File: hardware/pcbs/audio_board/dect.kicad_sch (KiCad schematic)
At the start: 9 parts, among them M1 DHAN-M_Module

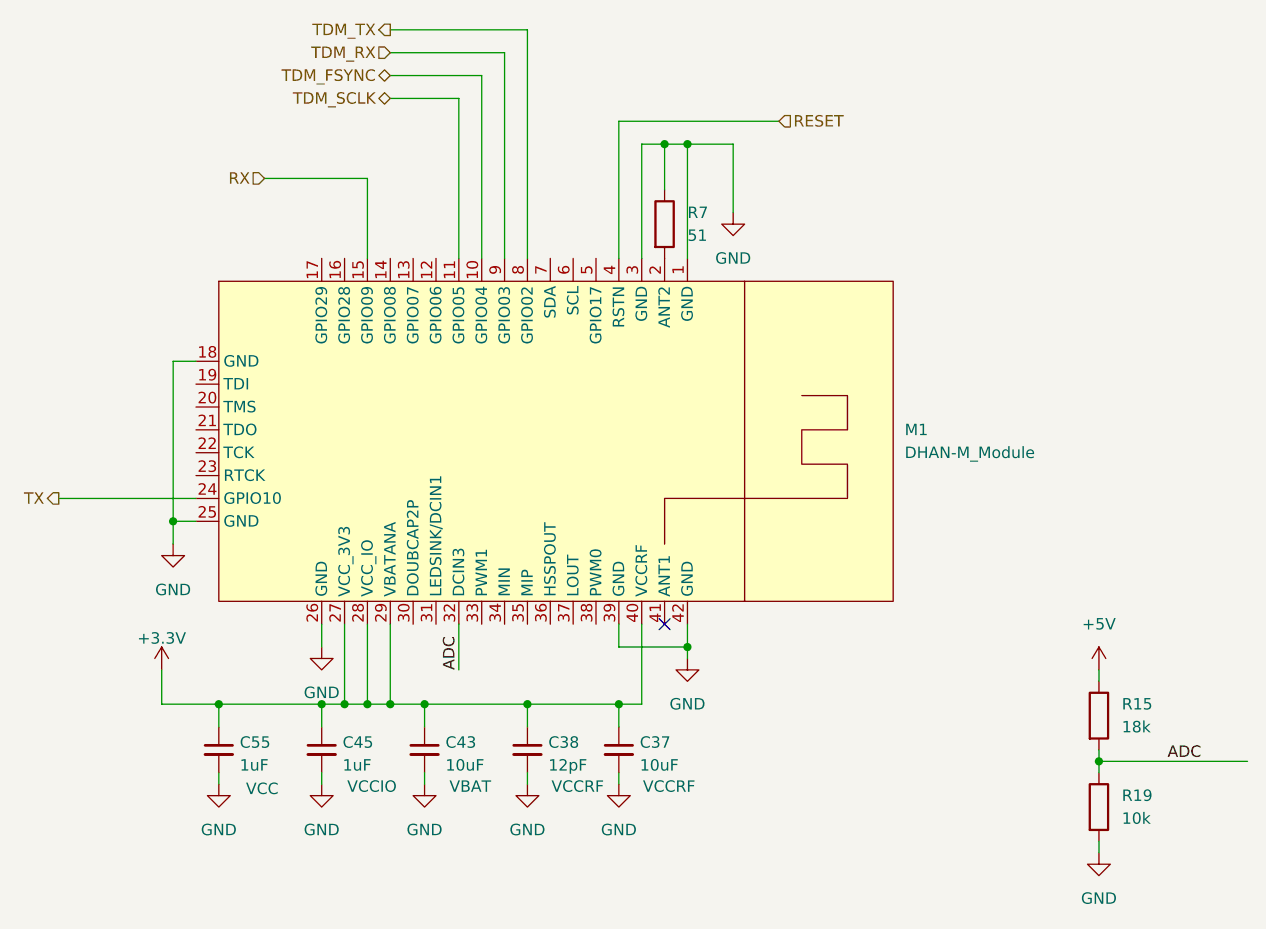
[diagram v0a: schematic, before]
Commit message: audio_board: Rework for DECT plug-in module
Redesigned the DECT area to accept a daughterboard with whatever DECT
module ends up working. Added more holes and silkscreen to make the
board neater.
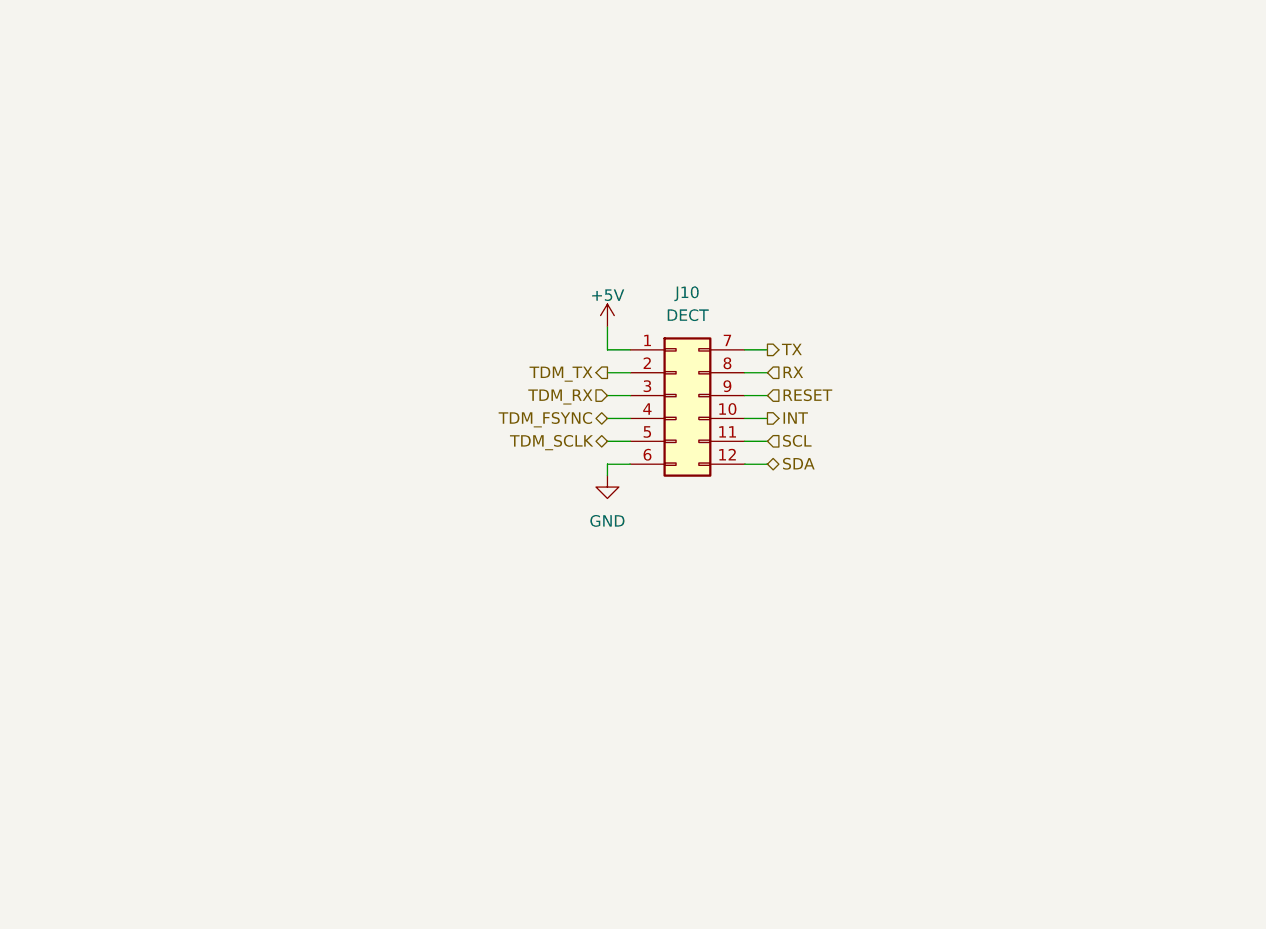
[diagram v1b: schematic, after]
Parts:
- removed C37, C43: 10uF, Capacitor_SMD:C_0805_2012Metric_Pad1.18x1.45mm_HandSolder, symbol Device:C_Small
- removed C38: 12pF, Capacitor_SMD:C_0603_1608Metric_Pad1.08x0.95mm_HandSolder, symbol Device:C_Small
- removed C45, C55: 1uF, Capacitor_SMD:C_0603_1608Metric_Pad1.08x0.95mm_HandSolder, symbol Device:C_Small
- removed M1: DHAN-M_Module, Library:DHAN-M_Module, symbol Parts:DHAN-M_Module
- removed R15: 18k, Resistor_SMD:R_0603_1608Metric_Pad0.98x0.95mm_HandSolder, symbol Device:R
- removed R19: 10k, Resistor_SMD:R_0603_1608Metric_Pad0.98x0.95mm_HandSolder, symbol Device:R
- removed R7: 51, Resistor_SMD:R_0603_1608Metric_Pad0.98x0.95mm_HandSolder, symbol Device:R
- added J10: DECT, Library:DectModule, symbol Connector_Generic:Conn_02x06_Top_Bottom
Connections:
- net +5V: now also J10.1 (Pin_1)
- net GND: now also J10.6 (Pin_6)
- net RESET: now also J10.9 (Pin_9)
- net RX: now also J10.8 (Pin_8)
- net TDM_FSYNC: now also J10.4 (Pin_4)
- net TDM_RX: now also J10.3 (Pin_3)
- net TDM_SCLK: now also J10.5 (Pin_5)
- net TDM_TX: now also J10.2 (Pin_2)
- net TX: now also J10.7 (Pin_7)
- new net INT: J10.10 (Pin_10)
- new net SCL: J10.11 (Pin_11)
- new net SDA: J10.12 (Pin_12)
- no-connect marks 1 -> 0

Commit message: audio_board, power_board: update shop and part links
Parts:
- J10: Part (none) -> 2x Header_2x06
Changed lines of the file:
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@@
+			)
+		)
+		(property "Part" "2x Header_2x06"
+			(at 153.67 99.06 0)
+			(effects
+				(font
+					(size 1.27 1.27)
+				)
+				(hide yes)
 			)
 		)

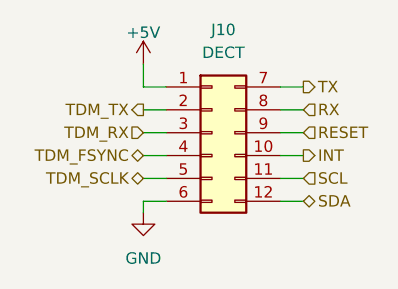
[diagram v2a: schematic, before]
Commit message: Audio board revision C
* Switched the neutrik jacks to NC3FAH2 instead of FAH1 so the jacks
  with an extra ground pin fit (but the FAH1 ones also still fit)
* Added traces for optional leds (marked DNP)
* Fixed up the opamp orientation for the XLR outputs
* Moved the LCD connector to the other side of the board and switched to
  an MTA-100 connector
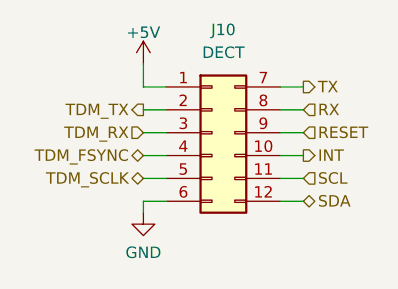
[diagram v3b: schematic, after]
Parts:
- J10: Part 2x Header_2x06 -> (none)
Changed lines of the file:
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@@
-	)
-	(symbol
-		(lib_id "power:GND")
-		(at 146.05 107.95 0)
-		(unit 1)
-		(exclude_from_sim no)
-		(in_bom yes)
-		(on_board yes)
-		(dnp no)
-		(fields_autoplaced yes)
-		(property "Reference" "#PWR033"
-			(at 146.05 114.3 0)
-			(effects
-				(font
-					(size 1.27 1.27)
-				)
-				(hide yes)
-			)
-		)
-		(property "Value" "GND"
-			(at 146.05 113.03 0)
-			(effects
-				(font
-					(size 1.27 1.27)
-				)
-			)
-		)
-		(property "Footprint" ""
-			(at 146.05 107.95 0)
-			(effects
-				(font
-					(size 1.27 1.27)
-				)
-				(hide yes)
-			)
-		)
-		(property "Datasheet" ""
-			(at 146.05 107.95 0)
-			(effects
-				(font
-					(size 1.27 1.27)
-				)
-				(hide yes)
-			)
-		)
-		(property "Description" "Power symbol creates a global label with name \"GND\" , ground"
-			(at 146.05 107.95 0)
-			(effects
-				(font
-					(size 1.27 1.27)
-				)
-				(hide yes)
-			)
-		)
-		(pin "1"
-		)
-		(instances
-			(project "audio_board"
-				(path "/54443f96-c7c5-4432-b890-45b14a1547a1/c4fe3322-408e-4a63-9af2-adca55ba4923"
-					(reference "#PWR033")
-					(unit 1)
-				)
-			)
-		)
 	)
 	(symbol
@@
 			)
 		)
-		(property "Part" "2x Header_2x06"
-			(at 153.67 99.06 0)
-			(effects
-				(font
-					(size 1.27 1.27)
-				)
-				(hide yes)
-			)
-		)
 		(pin "12"
 		)
@@
 					(unit 1)
 				)
+			)
+		)
+	)
+	(symbol
+		(lib_id "power:GND")
+		(at 146.05 107.95 0)
+		(unit 1)
+		(exclude_from_sim no)
+		(in_bom yes)
+		(on_board yes)
+		(dnp no)
+		(fields_autoplaced yes)
+		(property "Reference" "#PWR033"
+			(at 146.05 114.3 0)
+			(effects
+				(font
+					(size 1.27 1.27)
+				)
+				(hide yes)
+			)
+		)
+		(property "Value" "GND"
+			(at 146.05 112.3934 0)
+			(effects
+				(font
+					(size 1.27 1.27)
+				)
+			)
+		)
+		(property "Footprint" ""
+			(at 146.05 107.95 0)
+			(effects
+				(font
+					(size 1.27 1.27)
+				)
+				(hide yes)
+			)
+		)
+		(property "Datasheet" ""
+			(at 146.05 107.95 0)
+			(effects
+				(font
+					(size 1.27 1.27)
+				)
+				(hide yes)
+			)
+		)
+		(property "Description" ""
+			(at 146.05 107.95 0)
+			(effects
+				(font
+					(size 1.27 1.27)
+				)
+				(hide yes)
+			)
+		)
+		(pin "1"
+		)
+		(instances
+			(project "audio_board"
+				(path "/54443f96-c7c5-4432-b890-45b14a1547a1/c4fe3322-408e-4a63-9af2-adca55ba4923"
+					(reference "#PWR033")
+					(unit 1)
+				)

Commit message: pcbs: update purchase info
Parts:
- J10: Part (none) -> 2x Header_1x06
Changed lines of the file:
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@@
+			)
+		)
+		(property "Part" "2x Header_1x06"
+			(at 153.67 99.06 0)
+			(effects
+				(font
+					(size 1.27 1.27)
+				)
+				(hide yes)
 			)
 		)
